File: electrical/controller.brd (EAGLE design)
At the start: 101.6 x 25.4 mm, 44 parts, among them IC1 555, IC2 MCP4728, J3 455-1750-1-ND, Q1 DMP3098, Q2 DMG3402L-7, Q3 600mA/40V, Q4 DMP3098, U1 U3V16F15, U2 U3V16F15, U5 MCP6042, U6 MCP6042

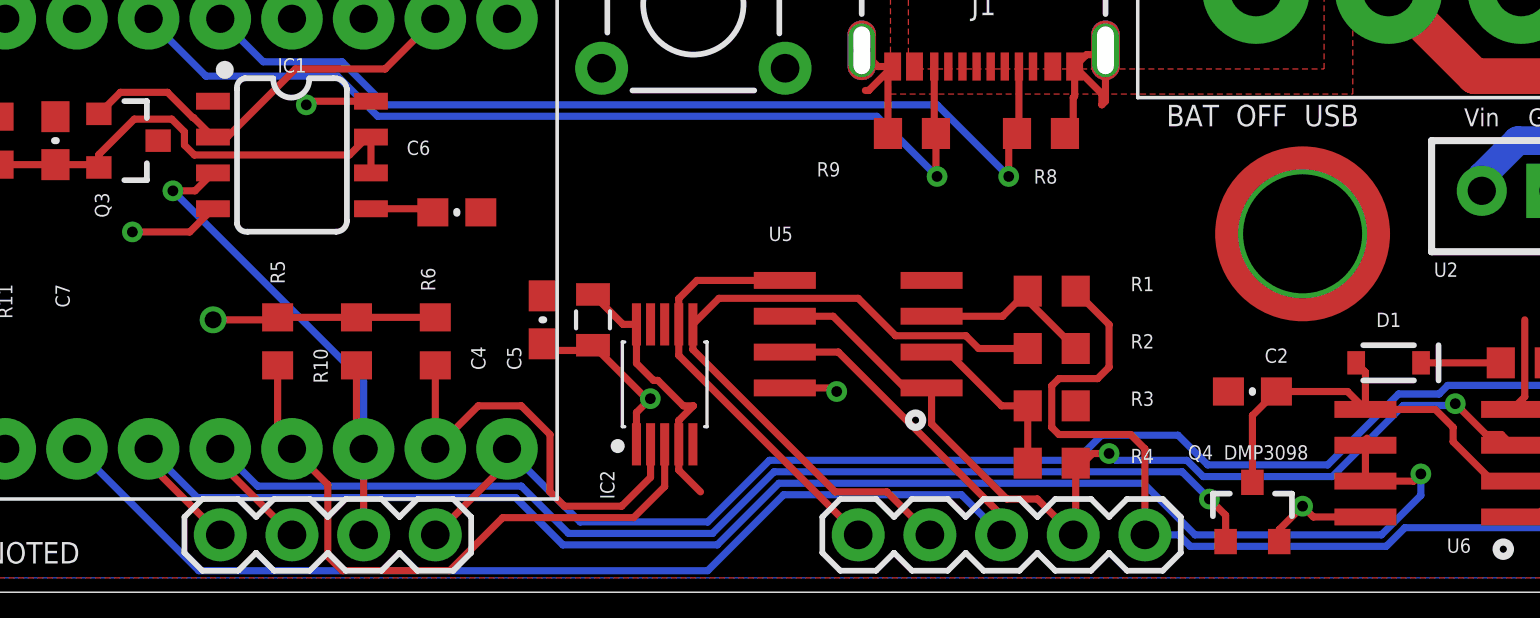
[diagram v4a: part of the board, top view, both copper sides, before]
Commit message: Calculate resistor values for new coil
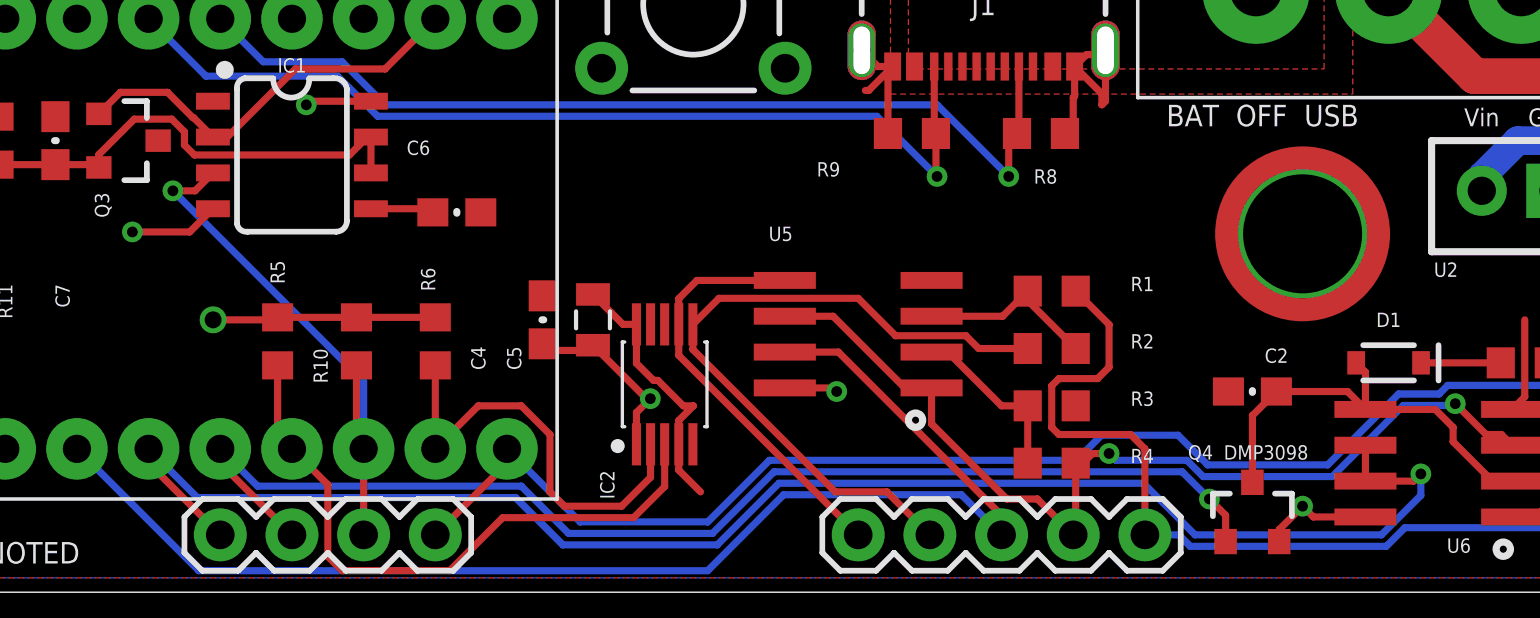
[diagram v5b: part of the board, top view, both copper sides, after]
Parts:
- R1: value 10K -> 16.6k
- R2: value 10K -> 3.3k
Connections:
- net !DRIVE renamed TIMER_RST
- net AUTO_RESTART renamed TIMER_RESTART
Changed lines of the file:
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@@
 <attribute name="VALUE" x="55.88" y="12.827" size="0.508" layer="27" font="vector" ratio="18" rot="R180"/>
 </element>
-<element name="R2" library="pie" package="R0603" value="10K" x="60.96" y="8.636" smashed="yes">
+<element name="R2" library="pie" package="R0603" value="3.3k" x="60.96" y="8.636" smashed="yes">
 <attribute name="DESCRIPTION" value="RESISTOR, American symbol" x="107.95" y="-44.704" size="1.778" layer="27" display="off"/>
 <attribute name="DISTRIBUTOR" value="DigiKey" x="107.95" y="-44.704" size="1.778" layer="27" display="off"/>
@@
 <attribute name="PACKAGE" value="R0603" x="3.81" y="57.912" size="1.778" layer="27" rot="R180" display="off"/>
 </element>
-<element name="R1" library="pie" package="R0603" value="10K" x="60.96" y="10.668" smashed="yes" rot="R180">
+<element name="R1" library="pie" package="R0603" value="16.6k" x="60.96" y="10.668" smashed="yes" rot="R180">
 <attribute name="DESCRIPTION" value="RESISTOR, American symbol" x="44.45" y="70.358" size="1.778" layer="27" rot="R180" display="off"/>
 <attribute name="DISTRIBUTOR" value="DigiKey" x="44.45" y="70.358" size="1.778" layer="27" rot="R180" display="off"/>
@@
 <wire x1="38.901" y1="13.589" x2="39.028" y2="13.462" width="0.254" layer="1"/>
 </signal>
-<signal name="AUTO_RESTART">
-<contactref element="IC1" pad="3"/>
-<contactref element="UC1" pad="7"/>
-<contactref element="R10" pad="2"/>
-<wire x1="36.322" y1="8.04" x2="36.322" y2="5.334" width="0.254" layer="1"/>
-<wire x1="36.322" y1="5.334" x2="36.576" y2="5.08" width="0.254" layer="1"/>
-<via x="29.8167" y="14.224" extent="1-16" drill="0.381"/>
-<wire x1="31.236" y1="14.859" x2="30.601" y2="14.224" width="0.254" layer="1"/>
-<wire x1="30.601" y1="14.224" x2="29.8167" y2="14.224" width="0.254" layer="1"/>
-<wire x1="29.8167" y1="14.224" x2="36.576" y2="7.4647" width="0.254" layer="16"/>
-<wire x1="36.576" y1="7.4647" x2="36.576" y2="5.08" width="0.254" layer="16"/>
-<contactref element="J5" pad="2"/>
-<wire x1="36.576" y1="5.08" x2="36.576" y2="2.032" width="0.254" layer="1"/>
-</signal>
 <signal name="N$7">
 <contactref element="IC1" pad="7"/>
@@
 <wire x1="30.57586875" y1="15.494" x2="36.074" y2="15.494" width="0.254" layer="1"/>
 <wire x1="25.654" y1="15.152" x2="23.622" y2="15.152" width="0.254" layer="1"/>
-</signal>
-<signal name="!DRIVE">
-<contactref element="UC1" pad="16"/>
-<contactref element="IC1" pad="2"/>
-<contactref element="Q3" pad="1"/>
-<wire x1="31.236" y1="16.129" x2="31.744" y2="16.129" width="0.254" layer="1"/>
-<wire x1="34.157" y1="18.542" x2="31.744" y2="16.129" width="0.254" layer="1"/>
-<wire x1="37.338" y1="18.542" x2="39.116" y2="20.32" width="0.254" layer="1"/>
-<wire x1="34.157" y1="18.542" x2="37.338" y2="18.542" width="0.254" layer="1"/>
-<wire x1="29.62586875" y1="17.714" x2="27.956" y2="17.714" width="0.254" layer="1"/>
-<wire x1="27.194" y1="16.952" x2="27.956" y2="17.714" width="0.254" layer="1"/>
-<wire x1="29.62586875" y1="17.714" x2="30.52026875" y2="16.8196" width="0.254" layer="1"/>
-<wire x1="30.52026875" y1="16.8196" x2="30.5454" y2="16.8196" width="0.254" layer="1"/>
-<wire x1="30.5454" y1="16.8196" x2="31.236" y2="16.129" width="0.254" layer="1"/>
-<contactref element="J3" pad="1"/>
-<wire x1="34.036" y1="23.368" x2="36.068" y2="23.368" width="0.254" layer="1"/>
-<wire x1="36.068" y1="23.368" x2="39.116" y2="20.32" width="0.254" layer="1"/>
 </signal>
 <signal name="VIN">
@@
 <wire x1="49.1076625" y1="1.6764" x2="51.2920625" y2="3.8608" width="0.254" layer="16"/>
 <via x="74.041" y="4.191" extent="1-16" drill="0.381"/>
-<wire x1="72.076" y1="5.401" x2="72.076" y2="5.207" width="0.254" layer="1"/>
 <wire x1="43.6372" y1="1.6764" x2="49.1076625" y2="1.6764" width="0.254" layer="16"/>
 <wire x1="72.076" y1="3.937" x2="72.076" y2="5.207" width="0.254" layer="1"/>
-<wire x1="72.076" y1="5.401" x2="72.136" y2="5.461" width="0.254" layer="1"/>
 <wire x1="51.2920625" y1="3.8608" x2="64.2112" y2="3.8608" width="0.254" layer="16"/>
 <wire x1="66.04" y1="2.032" x2="72.644" y2="2.032" width="0.254" layer="16"/>
@@
 <wire x1="31.496" y1="2.032" x2="28.956" y2="4.572" width="0.254" layer="1"/>
 </signal>
+<signal name="TIMER_RST">
+<contactref element="UC1" pad="16"/>
+<contactref element="IC1" pad="2"/>
+<contactref element="Q3" pad="1"/>
+<wire x1="31.236" y1="16.129" x2="31.744" y2="16.129" width="0.254" layer="1"/>
+<wire x1="34.157" y1="18.542" x2="31.744" y2="16.129" width="0.254" layer="1"/>
+<wire x1="34.157" y1="18.542" x2="37.338" y2="18.542" width="0.254" layer="1"/>
+<wire x1="29.62586875" y1="17.714" x2="27.956" y2="17.714" width="0.254" layer="1"/>
+<wire x1="27.194" y1="16.952" x2="27.956" y2="17.714" width="0.254" layer="1"/>
+<wire x1="29.62586875" y1="17.714" x2="30.52026875" y2="16.8196" width="0.254" layer="1"/>
+<wire x1="30.52026875" y1="16.8196" x2="30.5454" y2="16.8196" width="0.254" layer="1"/>
+<wire x1="30.5454" y1="16.8196" x2="31.236" y2="16.129" width="0.254" layer="1"/>
+<contactref element="J3" pad="1"/>
+<wire x1="34.036" y1="23.368" x2="36.068" y2="23.368" width="0.254" layer="1"/>
+<wire x1="36.068" y1="23.368" x2="39.116" y2="20.32" width="0.254" layer="1"/>
+<wire x1="37.338" y1="18.542" x2="39.116" y2="20.32" width="0.254" layer="1"/>
+</signal>
+<signal name="TIMER_RESTART">
+<contactref element="IC1" pad="3"/>
+<contactref element="R10" pad="2"/>
+<contactref element="UC1" pad="7"/>
+<wire x1="36.322" y1="5.334" x2="36.576" y2="5.08" width="0.254" layer="1"/>
+<via x="29.8167" y="14.224" extent="1-16" drill="0.381"/>
+<wire x1="29.8167" y1="14.224" x2="30.601" y2="14.224" width="0.254" layer="1"/>
+<wire x1="29.8167" y1="14.224" x2="36.576" y2="7.4647" width="0.254" layer="16"/>
+<wire x1="36.576" y1="7.4647" x2="36.576" y2="5.08" width="0.254" layer="16"/>
+<contactref element="J5" pad="2"/>
+<wire x1="36.576" y1="5.08" x2="36.576" y2="2.032" width="0.254" layer="1"/>
+<wire x1="30.601" y1="14.224" x2="31.236" y2="14.859" width="0.254" layer="1"/>
+<wire x1="36.322" y1="8.04" x2="36.322" y2="5.334" width="0.254" layer="1"/>
+</signal>
 </signals>

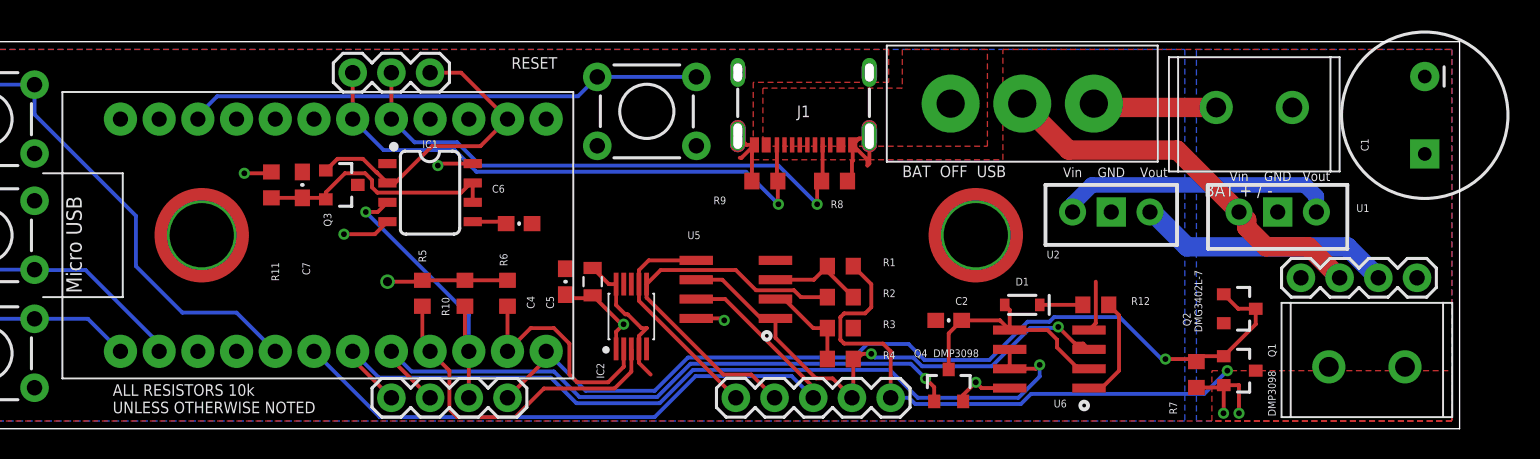
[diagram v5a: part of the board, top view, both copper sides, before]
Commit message: Added resistor arrays + other minor erratta, ready for prod
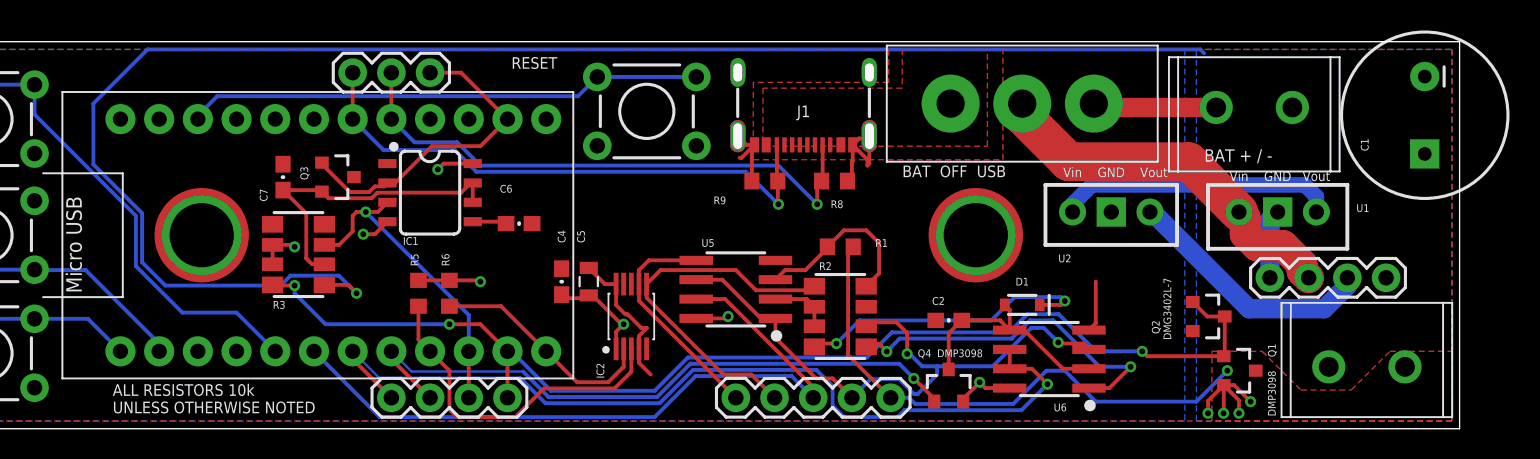
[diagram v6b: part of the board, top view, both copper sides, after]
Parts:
- removed R10, R7: 1M, pie:R0603
- removed R11: 2.2M, pie:R0603
- removed R12: 22k, pie:R0603
- removed R4: 10K, pie:R0603
- C7: value 2.2uf -> 4.7uF
- R1: value 16.6k -> 110k
- R2: value 3.3k -> 22k; device pie:R0603 -> BEST_Custom:2012-ARV
- R3: value 10K -> 1M; device pie:R0603 -> BEST_Custom:2012-ARV
- U5, U6: device linear:SO08 -> BEST_Custom:SO08
- moved R3 35.9 mm to (25.4, 11.4), turned to 90 degrees
- moved R6 3.81 mm to (35.3, 8.89)
- moved Q2 2.09 mm to (85.1, 7.37)
- moved J2 2.03 mm to (89.2, 9.91)
- moved C7 1.37 mm to (24.4, 16.5)
- moved R1 1.27 mm to (61.0, 11.9)
- moved R2 1.27 mm to (61.0, 7.37), turned to 90 degrees
- moved Q3 0.57 mm to (27.9, 16.5)
- moved C4 0.25 mm to (42.7, 9.65)
- moved C5 0.25 mm to (44.5, 9.65)
- moved R5 0.25 mm to (33.3, 8.89)
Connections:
- net 15V: now also R3.1; no longer R7.2
- net 5V: now also R3.6, R3.7; no longer R10.1, R11.2
- net DRIVE: now also R3.8, UC1.8; no longer R7.1, UC1.9
- net GND: now also R2.3; no longer R3.2
- net N$2: now also R2.1; no longer R12.1
- net N$3: now also R2.8; no longer R12.2
- net N$4: now also R2.4; no longer R2.2
- net N$5: now also R2.6, R2.7; no longer R3.1, R4.2
- net N$7: now also R3.2; no longer R11.1
- net SCL: now also UC1.9; no longer UC1.8
- net SHIFT: now also R2.2; no longer R4.1
- net TIMER_RESTART: now also R3.3; no longer R10.2
- net V1: now also R2.5; no longer R2.1
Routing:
- net 15V: track 25.0 -> 131.1 mm, vias 2 -> 5
- net N$3: track 2.83 -> 19.6 mm, vias 0 -> 2
- net DRIVE: track 60.6 -> 77.0 mm, vias 1 -> 3
- net N$2: track 7.04 -> 23.1 mm, vias 0 -> 2
- net SHIFT: track 34.4 -> 40.1 mm
- net N$4: track 6.51 -> 11.7 mm
- net GND: track 25.6 -> 30.3 mm
- net N$7: track 16.7 -> 21.0 mm
- net 5V: track 44.5 -> 40.7 mm
- net N$5: track 6.23 -> 4.04 mm
- net A_PEAK: track 56.9 -> 59.1 mm
- net TIMER_RESTART: track 19.7 -> 20.9 mm
- net VIN: track 25.9 -> 24.8 mm
- net V1: track 25.0 -> 24.1 mm
- net COIL: track 36.8 -> 36.1 mm
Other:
- board text added: "15V 5V VIN GND"
- board text added: "COIL SHIFT INT V1 V2"
- board text added: "DRIVE TIMER_RESTART PEAK_RESET A_PEAK"
- board text added: "Douglas Hutchings Double Pendulum Driver Rev D2 7-21-25"
- board text added: "TIMER_RST CC1 CC2"
- board text removed: "Douglas Hutchings Double Pendulum Driver Rev D2"

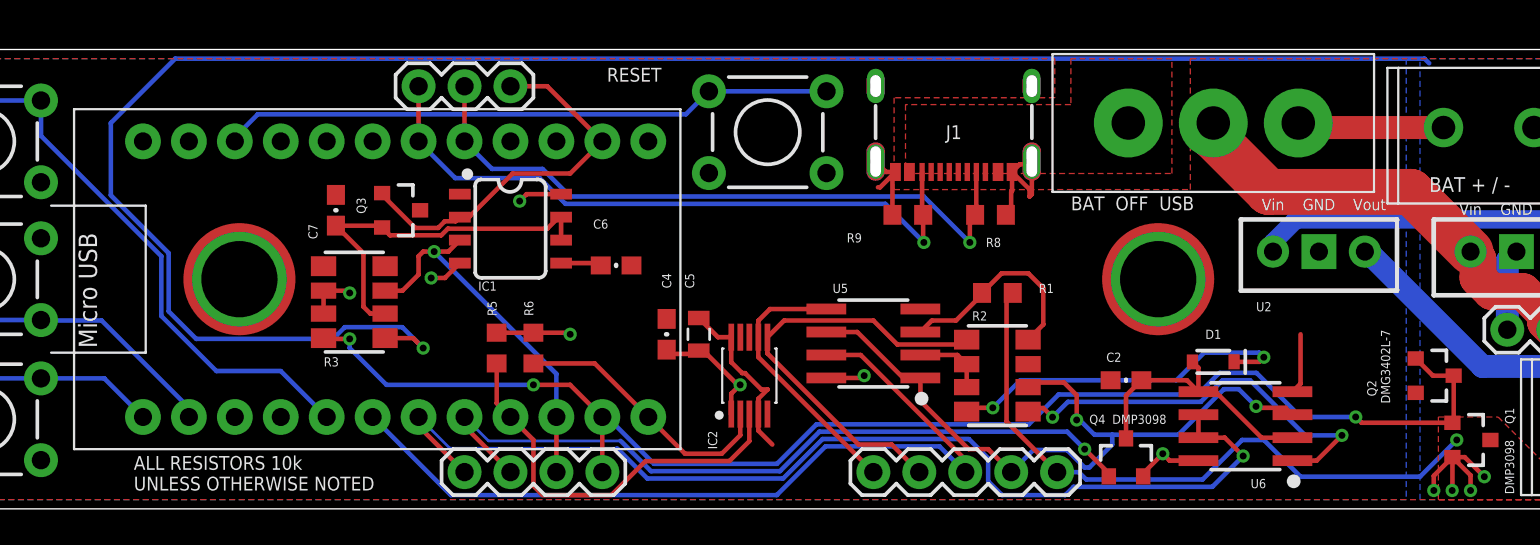
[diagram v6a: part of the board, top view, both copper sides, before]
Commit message: Add missing pullup; tweak slots for JLCPCB fab
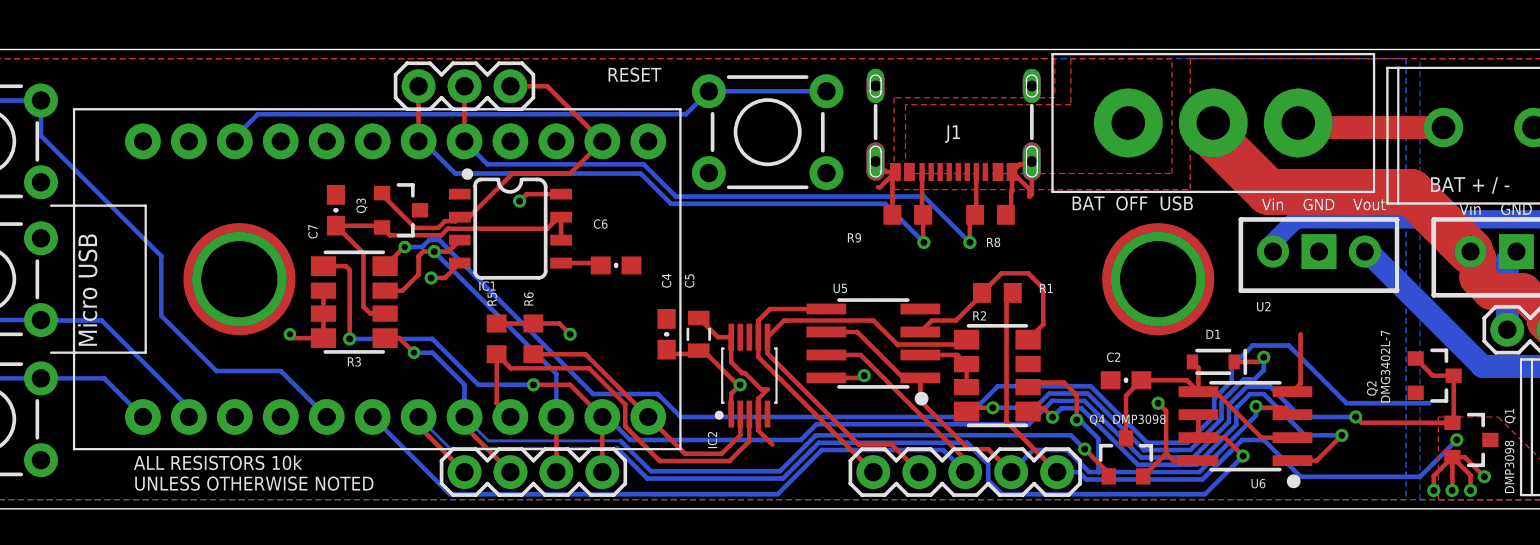
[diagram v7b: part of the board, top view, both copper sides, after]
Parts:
- moved R5 0.51 mm to (33.3, 9.40)
- moved R6 0.51 mm to (35.3, 9.40)
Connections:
- net 15V: now also R3.4; no longer R3.1
- net 5V: now also R3.8
- net DRIVE: now also R3.5; no longer R3.8
- net PEAK_RST: now also R3.1
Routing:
- net 15V: track 131.1 -> 96.1 mm
- net PEAK_RST: track 43.0 -> 50.1 mm, vias 1 -> 2
- net DRIVE: track 77.0 -> 82.0 mm
- net 5V: track 40.7 -> 45.6 mm
- net N$3: track 19.6 -> 23.0 mm
- net N$2: track 23.1 -> 25.6 mm
- net SHIFT: track 40.1 -> 40.7 mm
